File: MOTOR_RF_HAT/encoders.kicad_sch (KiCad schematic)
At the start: 14 parts, among them J2 JST_EL, J3 END_AZ, J6 JST_AZ, J7 END_EL

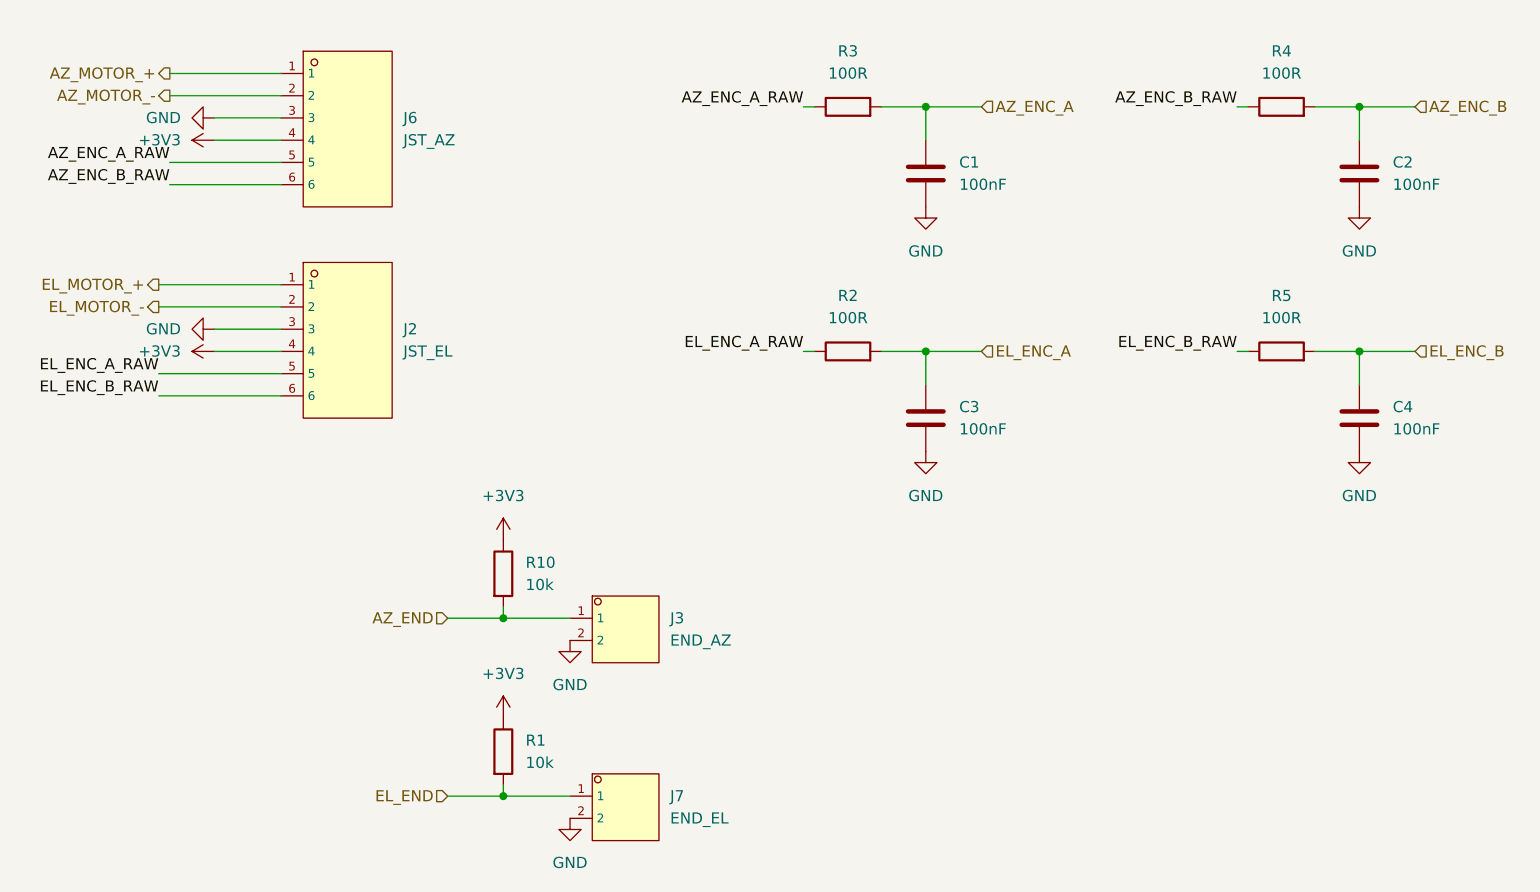
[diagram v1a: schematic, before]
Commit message: MOTOR_RF_HAT: fix TestPoint:smallpad → components:smallpad in solder_pads
All 18 test point footprint references in solder_pads.kicad_sch now
point to the local components:smallpad instead of TestPoint:smallpad
(which doesn't exist in KiCad's global TestPoint library).

Co-Authored-By: Claude Opus 4.6 (1M context) <noreply@anthropic.com>
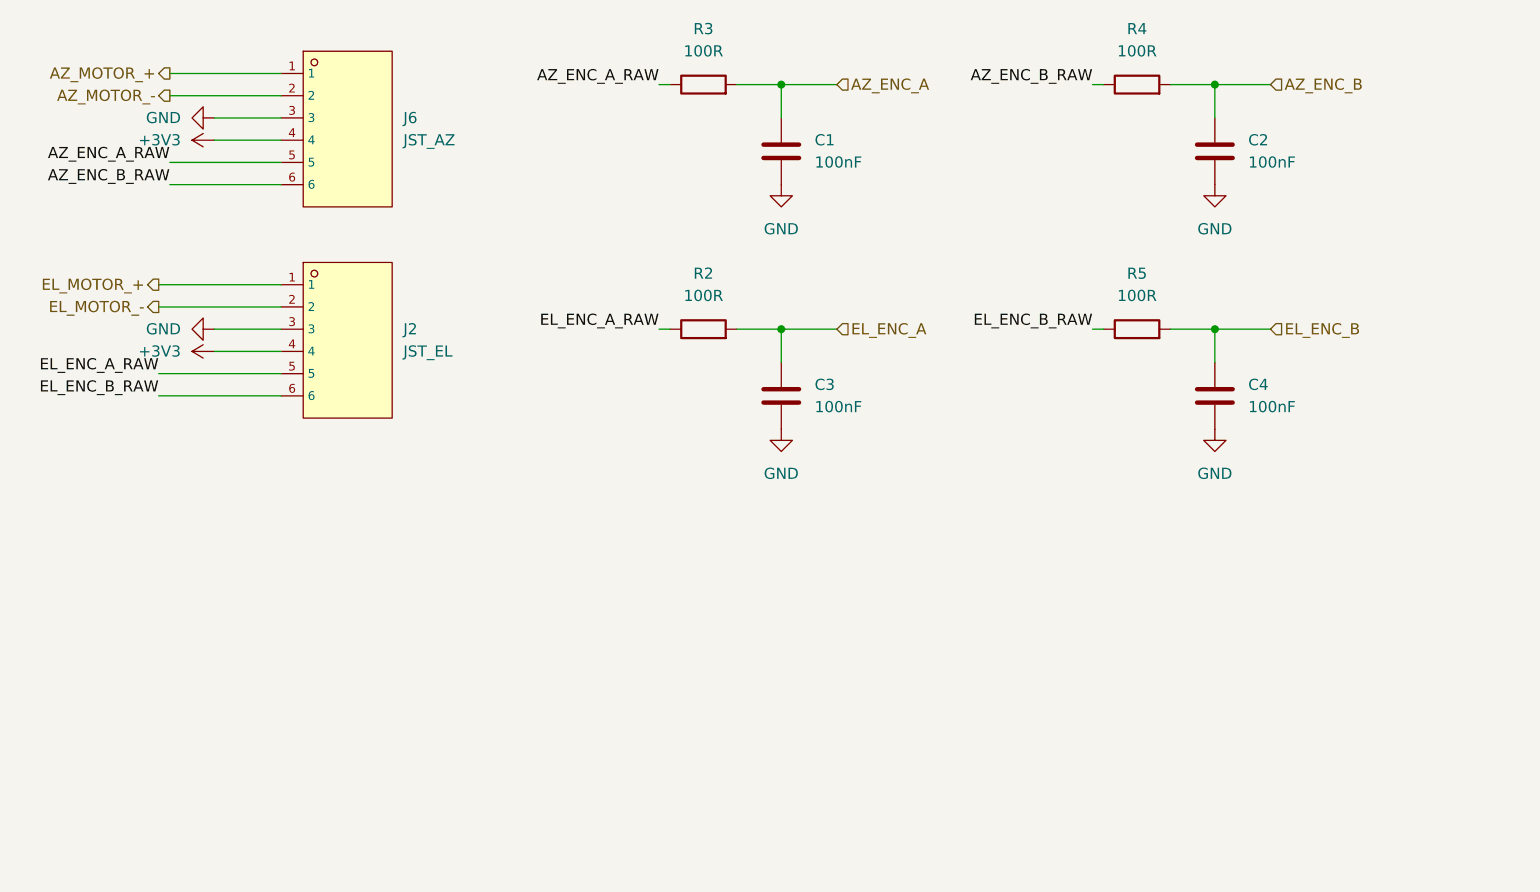
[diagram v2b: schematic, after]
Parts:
- removed J3: END_AZ, components:CONN-TH_S2B-XH-A-LF-SN, symbol components:S2B-XH-A-(LF)(SN)
- removed J7: END_EL, components:CONN-TH_S2B-XH-A-LF-SN, symbol components:S2B-XH-A-(LF)(SN)
- removed R1, R10: 10k, Resistor_SMD:R_0805_2012Metric_Pad1.20x1.40mm_HandSolder, symbol Device:R
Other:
- moved on the sheet: C1, C2, C3, C4, R2, R3, R4, R5

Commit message: MOTOR_RF_HAT: add TestPoint lib alias to fix persistent smallpad errors
KiCad's lib_symbols cache keeps reverting footprint refs to
TestPoint:smallpad on save. Added TestPoint as a footprint library
alias pointing to components.pretty so both TestPoint:smallpad and
components:smallpad resolve to the same local footprint.

Co-Authored-By: Claude Opus 4.6 (1M context) <noreply@anthropic.com>
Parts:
- renumbered C1 to C68, C3 to C69, C2 to C70, C4 to C71, J2 to J7, R3 to R11, R2 to R12, R4 to R13, R5 to R14
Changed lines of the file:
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@@
 		(dnp no)
 		(fields_autoplaced yes)
-		(property "Reference" "C2"
+		(property "Reference" "C70"
 			(at 162.56 30.4799 0)
 			(show_name no)
@@
 			(project "MOTOR_RF_HAT"
 				(path "/300cf3d4-e317-44c8-acd8-5f9989779c7c/baddf2fd-a49c-44bc-8ff5-dce9cf0b07cd"
-					(reference "C2")
+					(reference "C70")
 					(unit 1)
 				)
@@
 		(dnp no)
 		(fields_autoplaced yes)
-		(property "Reference" "C4"
+		(property "Reference" "C71"
 			(at 162.56 58.4199 0)
 			(show_name no)
@@
 			(project "MOTOR_RF_HAT"
 				(path "/300cf3d4-e317-44c8-acd8-5f9989779c7c/baddf2fd-a49c-44bc-8ff5-dce9cf0b07cd"
-					(reference "C4")
+					(reference "C71")
 					(unit 1)
 				)
@@
 		(dnp no)
 		(fields_autoplaced yes)
-		(property "Reference" "C1"
+		(property "Reference" "C68"
 			(at 113.03 30.4799 0)
 			(show_name no)
@@
 			(project "MOTOR_RF_HAT"
 				(path "/300cf3d4-e317-44c8-acd8-5f9989779c7c/baddf2fd-a49c-44bc-8ff5-dce9cf0b07cd"
-					(reference "C1")
+					(reference "C68")
 					(unit 1)
 				)
@@
 		(dnp no)
 		(fields_autoplaced yes)
-		(property "Reference" "#PWR015"
+		(property "Reference" "#PWR066"
 			(at 38.1 27.94 0)
 			(hide yes)
@@
 			(project "MOTOR_RF_HAT"
 				(path "/300cf3d4-e317-44c8-acd8-5f9989779c7c/baddf2fd-a49c-44bc-8ff5-dce9cf0b07cd"
-					(reference "#PWR015")
+					(reference "#PWR066")
 					(unit 1)
 				)
@@
 		(dnp no)
 		(fields_autoplaced yes)
-		(property "Reference" "J2"
+		(property "Reference" "J7"
 			(at 66.04 52.0699 0)
 			(show_name no)
@@
 			(project "MOTOR_RF_HAT"
 				(path "/300cf3d4-e317-44c8-acd8-5f9989779c7c/baddf2fd-a49c-44bc-8ff5-dce9cf0b07cd"
-					(reference "J2")
+					(reference "J7")
 					(unit 1)
 				)
@@
 		(dnp no)
 		(fields_autoplaced yes)
-		(property "Reference" "#PWR021"
+		(property "Reference" "#PWR073"
 			(at 158.75 69.85 0)
 			(hide yes)
@@
 			(project "MOTOR_RF_HAT"
 				(path "/300cf3d4-e317-44c8-acd8-5f9989779c7c/baddf2fd-a49c-44bc-8ff5-dce9cf0b07cd"
-					(reference "#PWR021")
+					(reference "#PWR073")
 					(unit 1)
 				)
@@
 		(dnp no)
 		(fields_autoplaced yes)
-		(property "Reference" "R2"
+		(property "Reference" "R12"
 			(at 100.33 45.72 90)
 			(show_name no)
@@
 			(project "MOTOR_RF_HAT"
 				(path "/300cf3d4-e317-44c8-acd8-5f9989779c7c/baddf2fd-a49c-44bc-8ff5-dce9cf0b07cd"
-					(reference "R2")
+					(reference "R12")
 					(unit 1)
 				)
@@
 		(dnp no)
 		(fields_autoplaced yes)
-		(property "Reference" "#PWR016"
+		(property "Reference" "#PWR068"
 			(at 38.1 52.07 0)
 			(hide yes)
@@
 			(project "MOTOR_RF_HAT"
 				(path "/300cf3d4-e317-44c8-acd8-5f9989779c7c/baddf2fd-a49c-44bc-8ff5-dce9cf0b07cd"
-					(reference "#PWR016")
+					(reference "#PWR068")
 					(unit 1)
 				)
@@
 		(dnp no)
 		(fields_autoplaced yes)
-		(property "Reference" "R5"
+		(property "Reference" "R14"
 			(at 149.86 45.72 90)
 			(show_name no)
@@
 			(project "MOTOR_RF_HAT"
 				(path "/300cf3d4-e317-44c8-acd8-5f9989779c7c/baddf2fd-a49c-44bc-8ff5-dce9cf0b07cd"
-					(reference "R5")
+					(reference "R14")
 					(unit 1)
 				)
@@
 		(dnp no)
 		(fields_autoplaced yes)
-		(property "Reference" "C3"
+		(property "Reference" "C69"
 			(at 113.03 58.4199 0)
 			(show_name no)
@@
 			(project "MOTOR_RF_HAT"
 				(path "/300cf3d4-e317-44c8-acd8-5f9989779c7c/baddf2fd-a49c-44bc-8ff5-dce9cf0b07cd"
-					(reference "C3")
+					(reference "C69")
 					(unit 1)
 				)
@@
 		(dnp no)
 		(fields_autoplaced yes)
-		(property "Reference" "#PWR019"
+		(property "Reference" "#PWR072"
 			(at 158.75 41.91 0)
 			(hide yes)
@@
 			(project "MOTOR_RF_HAT"
 				(path "/300cf3d4-e317-44c8-acd8-5f9989779c7c/baddf2fd-a49c-44bc-8ff5-dce9cf0b07cd"
-					(reference "#PWR019")
+					(reference "#PWR072")
 					(unit 1)
 				)
@@
 		(dnp no)
 		(fields_autoplaced yes)
-		(property "Reference" "#PWR018"
+		(property "Reference" "#PWR070"
 			(at 109.22 41.91 0)
 			(hide yes)
@@
 			(project "MOTOR_RF_HAT"
 				(path "/300cf3d4-e317-44c8-acd8-5f9989779c7c/baddf2fd-a49c-44bc-8ff5-dce9cf0b07cd"
-					(reference "#PWR018")
+					(reference "#PWR070")
 					(unit 1)
 				)
@@
 		(dnp no)
 		(fields_autoplaced yes)
-		(property "Reference" "#PWR017"
+		(property "Reference" "#PWR067"
 			(at 48.26 30.48 0)
 			(hide yes)
@@
 			(project "MOTOR_RF_HAT"
 				(path "/300cf3d4-e317-44c8-acd8-5f9989779c7c/baddf2fd-a49c-44bc-8ff5-dce9cf0b07cd"
-					(reference "#PWR017")
+					(reference "#PWR067")
 					(unit 1)
 				)
@@
 		(dnp no)
 		(fields_autoplaced yes)
-		(property "Reference" "#PWR020"
+		(property "Reference" "#PWR071"
 			(at 109.22 69.85 0)
 			(hide yes)
@@
 			(project "MOTOR_RF_HAT"
 				(path "/300cf3d4-e317-44c8-acd8-5f9989779c7c/baddf2fd-a49c-44bc-8ff5-dce9cf0b07cd"
-					(reference "#PWR020")
+					(reference "#PWR071")
 					(unit 1)
 				)
@@
 		(dnp no)
 		(fields_autoplaced yes)
-		(property "Reference" "R3"
+		(property "Reference" "R11"
 			(at 100.33 17.78 90)
 			(show_name no)
@@
 			(project "MOTOR_RF_HAT"
 				(path "/300cf3d4-e317-44c8-acd8-5f9989779c7c/baddf2fd-a49c-44bc-8ff5-dce9cf0b07cd"
-					(reference "R3")
+					(reference "R11")
 					(unit 1)
 				)
@@
 		(dnp no)
 		(fields_autoplaced yes)
-		(property "Reference" "R4"
+		(property "Reference" "R13"
 			(at 149.86 17.78 90)
 			(show_name no)
@@
 			(project "MOTOR_RF_HAT"
 				(path "/300cf3d4-e317-44c8-acd8-5f9989779c7c/baddf2fd-a49c-44bc-8ff5-dce9cf0b07cd"
-					(reference "R4")
+					(reference "R13")
 					(unit 1)
 				)
@@
 		(dnp no)
 		(fields_autoplaced yes)
-		(property "Reference" "#PWR014"
+		(property "Reference" "#PWR069"
 			(at 48.26 54.61 0)
 			(hide yes)
@@
 			(project "MOTOR_RF_HAT"
 				(path "/300cf3d4-e317-44c8-acd8-5f9989779c7c/baddf2fd-a49c-44bc-8ff5-dce9cf0b07cd"
-					(reference "#PWR014")
-					(unit 1)
-				)
+					(reference "#PWR069")
+					(unit 1)
+				)

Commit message: MOTOR_RF_HAT: 0805→0603 passives, encoder caps 100nF→100pF
- Changed all capacitor and resistor footprints from 0805 to 0603
  across all schematic sheets (CC1200 UHF/VHF, root, azimuth,
  elevation, encoders)
- Fixed encoder RC filter caps C68-C71 from 100nF to 100pF
  (fc = 15.9 MHz, transparent to 35 kHz encoder signal)

Co-Authored-By: Claude Opus 4.6 (1M context) <noreply@anthropic.com>
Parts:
- C68, C69, C70, C71: value 100nF -> 100pF; footprint Capacitor_SMD:C_0805_2012Metric_Pad1.18x1.45mm_HandSolder -> Capacitor_SMD:C_0603_1608Metric
- R11, R12, R13, R14: footprint Resistor_SMD:R_0805_2012Metric_Pad1.20x1.40mm_HandSolder -> Resistor_SMD:R_0603_1608Metric
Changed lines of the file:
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@@
 			)
 		)
-		(property "Value" "100nF"
+		(property "Value" "100pF"
 			(at 162.56 33.0199 0)
 			(show_name no)
@@
 			)
 		)
-		(property "Footprint" "Capacitor_SMD:C_0805_2012Metric_Pad1.18x1.45mm_HandSolder"
+		(property "Footprint" "Capacitor_SMD:C_0603_1608Metric"
 			(at 159.7152 35.56 0)
 			(hide yes)
@@
 			)
 		)
-		(property "Value" "100nF"
+		(property "Value" "100pF"
 			(at 162.56 60.9599 0)
 			(show_name no)
@@
 			)
 		)
-		(property "Footprint" "Capacitor_SMD:C_0805_2012Metric_Pad1.18x1.45mm_HandSolder"
+		(property "Footprint" "Capacitor_SMD:C_0603_1608Metric"
 			(at 159.7152 63.5 0)
 			(hide yes)
@@
 			)
 		)
-		(property "Value" "100nF"
+		(property "Value" "100pF"
 			(at 113.03 33.0199 0)
 			(show_name no)
@@
 			)
 		)
-		(property "Footprint" "Capacitor_SMD:C_0805_2012Metric_Pad1.18x1.45mm_HandSolder"
+		(property "Footprint" "Capacitor_SMD:C_0603_1608Metric"
 			(at 110.1852 35.56 0)
 			(hide yes)
@@
 			)
 		)
-		(property "Footprint" "Resistor_SMD:R_0805_2012Metric_Pad1.20x1.40mm_HandSolder"
+		(property "Footprint" "Resistor_SMD:R_0603_1608Metric"
 			(at 100.33 53.848 90)
 			(hide yes)
@@
 			)
 		)
-		(property "Footprint" "Resistor_SMD:R_0805_2012Metric_Pad1.20x1.40mm_HandSolder"
+		(property "Footprint" "Resistor_SMD:R_0603_1608Metric"
 			(at 149.86 53.848 90)
 			(hide yes)
@@
 			)
 		)
-		(property "Value" "100nF"
+		(property "Value" "100pF"
 			(at 113.03 60.9599 0)
 			(show_name no)
@@
 			)
 		)
-		(property "Footprint" "Capacitor_SMD:C_0805_2012Metric_Pad1.18x1.45mm_HandSolder"
+		(property "Footprint" "Capacitor_SMD:C_0603_1608Metric"
 			(at 110.1852 63.5 0)
 			(hide yes)
@@
 			)
 		)
-		(property "Footprint" "Resistor_SMD:R_0805_2012Metric_Pad1.20x1.40mm_HandSolder"
+		(property "Footprint" "Resistor_SMD:R_0603_1608Metric"
 			(at 100.33 25.908 90)
 			(hide yes)
@@
 			)
 		)
-		(property "Footprint" "Resistor_SMD:R_0805_2012Metric_Pad1.20x1.40mm_HandSolder"
+		(property "Footprint" "Resistor_SMD:R_0603_1608Metric"
 			(at 149.86 25.908 90)
 			(hide yes)

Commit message: MOTOR_RF_HAT: BOM enrichment + design review fixes + firmware scaffold
BOM enrichment:
- Added LCSC, MPN, and Farnell properties to 122 of 131 components
  across all schematic sheets (remaining 9 are mechanical/test fixtures)
- Sourced all passives (0603 caps/resistors/inductors), ICs (CC1200,
  A4950E, LMR51420, BSS138, WS2812B), connectors (JST-XH, XT30, SMA)

Design review fixes:
- C1 (4.7uF 50V): 0805→1206 (physically impossible in 0805)
- R1/R2: fixed footprint library from Capacitor_SMD to Resistor_SMD

Firmware scaffold (Firmware/rp2040-motor-rf-hat/):
- Complete merged firmware: RF HAT base + rotator motor control
- motor_pwm.cpp refactored for 2-pin A4950 (IN1/IN2, no PWM pin)
- adxl345.cpp with SPI0 mode switching (mode 3 for IMU, mode 0 for VHF)
- proto.c extended with motor messages 0x60-0x69 (SET_POSITION, PARK,
  STOP, HOME, GET_STATUS, SET_GAINS, ZERO, IMU_READ, RECAL)
- Builds clean: 5.7% RAM, 4.2% flash
- Output: motor_rf_hat_firmware.uf2

Co-Authored-By: Claude Opus 4.6 (1M context) <noreply@anthropic.com>
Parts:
- C68, C69, C70, C71: LCSC (none) -> C14858; MPN (none) -> CL10C101JB8NNNC
- R11, R12, R13, R14: Farnell (none) -> 1469752; LCSC (none) -> C22775; MPN (none) -> 0603WAF1000T5E
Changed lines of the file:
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@@
+			)
+		)
+		(property "LCSC" "C14858"
+			(at 0 0 0)
+			(show_name no)
+			(do_not_autoplace no)
+			(hide yes)
+			(effects
+				(font
+					(size 1.27 1.27)
+				)
+			)
+		)
+		(property "MPN" "CL10C101JB8NNNC"
+			(at 0 0 0)
+			(show_name no)
+			(do_not_autoplace no)
+			(hide yes)
+			(effects
+				(font
+					(size 1.27 1.27)
+				)
 			)
 		)
@@
 			)
 		)
+		(property "LCSC" "C14858"
+			(at 0 0 0)
+			(hide yes)
+			(show_name no)
+			(do_not_autoplace no)
+			(effects (font (size 1.27 1.27)))
+		)
+		(property "MPN" "CL10C101JB8NNNC"
+			(at 0 0 0)
+			(hide yes)
+			(show_name no)
+			(do_not_autoplace no)
+			(effects (font (size 1.27 1.27)))
+		)
 		(pin "1"
 		)
@@
 				)
 			)
+		)
+		(property "LCSC" "C14858"
+			(at 0 0 0)
+			(hide yes)
+			(show_name no)
+			(do_not_autoplace no)
+			(effects (font (size 1.27 1.27)))
+		)
+		(property "MPN" "CL10C101JB8NNNC"
+			(at 0 0 0)
+			(hide yes)
+			(show_name no)
+			(do_not_autoplace no)
+			(effects (font (size 1.27 1.27)))
 		)
 		(pin "1"
@@
 			)
 		)
+		(property "LCSC" "C22775"
+			(at 0 0 0)
+			(hide yes)
+			(show_name no)
+			(do_not_autoplace no)
+			(effects (font (size 1.27 1.27)))
+		)
+		(property "MPN" "0603WAF1000T5E"
+			(at 0 0 0)
+			(hide yes)
+			(show_name no)
+			(do_not_autoplace no)
+			(effects (font (size 1.27 1.27)))
+		)
+		(property "Farnell" "1469752"
+			(at 0 0 0)
+			(hide yes)
+			(show_name no)
+			(do_not_autoplace no)
+			(effects (font (size 1.27 1.27)))
+		)
 		(pin "1"
 		)
@@
 			)
 		)
+		(property "LCSC" "C22775"
+			(at 0 0 0)
+			(hide yes)
+			(show_name no)
+			(do_not_autoplace no)
+			(effects (font (size 1.27 1.27)))
+		)
+		(property "MPN" "0603WAF1000T5E"
+			(at 0 0 0)
+			(hide yes)
+			(show_name no)
+			(do_not_autoplace no)
+			(effects (font (size 1.27 1.27)))
+		)
+		(property "Farnell" "1469752"
+			(at 0 0 0)
+			(hide yes)
+			(show_name no)
+			(do_not_autoplace no)
+			(effects (font (size 1.27 1.27)))
+		)
 		(pin "1"
 		)
@@
 			)
 		)
+		(property "LCSC" "C14858"
+			(at 0 0 0)
+			(hide yes)
+			(show_name no)
+			(do_not_autoplace no)
+			(effects (font (size 1.27 1.27)))
+		)
+		(property "MPN" "CL10C101JB8NNNC"
+			(at 0 0 0)
+			(hide yes)
+			(show_name no)
+			(do_not_autoplace no)
+			(effects (font (size 1.27 1.27)))
+		)
 		(pin "1"
 		)
@@
 			)
 		)
+		(property "LCSC" "C22775"
+			(at 0 0 0)
+			(hide yes)
+			(show_name no)
+			(do_not_autoplace no)
+			(effects (font (size 1.27 1.27)))
+		)
+		(property "MPN" "0603WAF1000T5E"
+			(at 0 0 0)
+			(hide yes)
+			(show_name no)
+			(do_not_autoplace no)
+			(effects (font (size 1.27 1.27)))
+		)
+		(property "Farnell" "1469752"
+			(at 0 0 0)
+			(hide yes)
+			(show_name no)
+			(do_not_autoplace no)
+			(effects (font (size 1.27 1.27)))
+		)
 		(pin "1"
 		)
@@
 			)
 		)
-		(pin "1"
+		(property "LCSC" "C22775"
+			(at 0 0 0)
+			(hide yes)
+			(show_name no)
+			(do_not_autoplace no)
+			(effects (font (size 1.27 1.27)))
+		)
+		(property "MPN" "0603WAF1000T5E"
+			(at 0 0 0)
+			(hide yes)
+			(show_name no)
+			(do_not_autoplace no)
+			(effects (font (size 1.27 1.27)))
+		)
+		(property "Farnell" "1469752"
+			(at 0 0 0)
+			(hide yes)
+			(show_name no)
+			(do_not_autoplace no)
+			(effects (font (size 1.27 1.27)))
+		)
+		(pin "1"
